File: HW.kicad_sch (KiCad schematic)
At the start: 0 parts

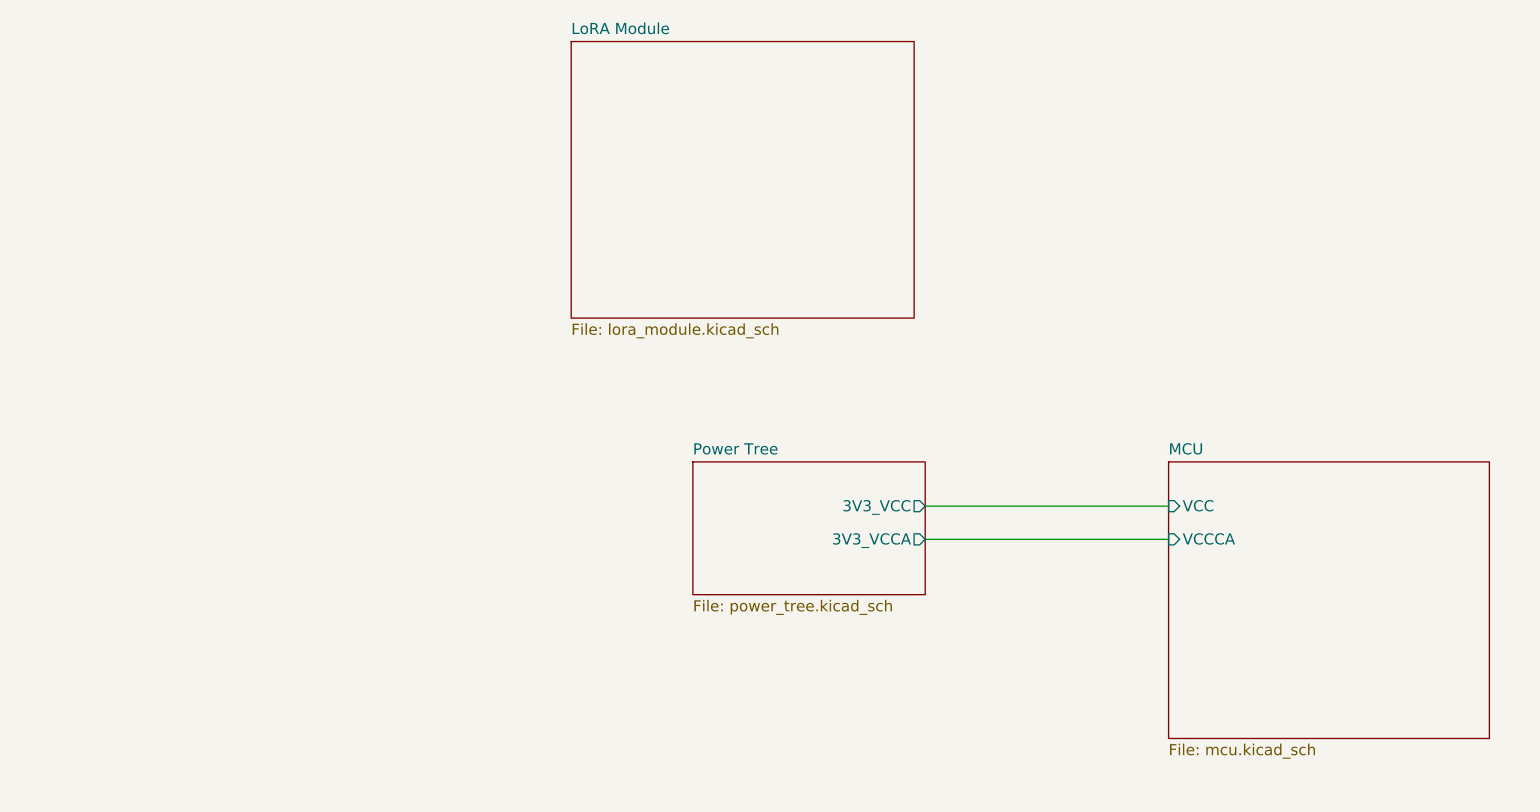
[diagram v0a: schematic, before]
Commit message: feat(usb-uart): add FT232RL USB‑UART bridge and wire RX/TX to MCU
Added the FT232RL USB‑to‑UART interface IC (FT232RL) into the schematic and powered it from the 3.3 V and 5 V rails. Exposed its TTL-level RXD and TXD pins through the hierarchical sheet and connected it to the MCU

- Placed FT232RL SSOP‑28 symbol and footprint, tied VCCIO to 3.3 V, VCC to USB_VCC, and GND to ground.
- Left legacy RS‑232 control lines (DSR#, DCD#, RI#) and CBUS pins unconnected.
- Updated hierarchy:added sheet pins on USB_UART page.

This enables USB‑serial communication between host PC and STM32F030F4Px
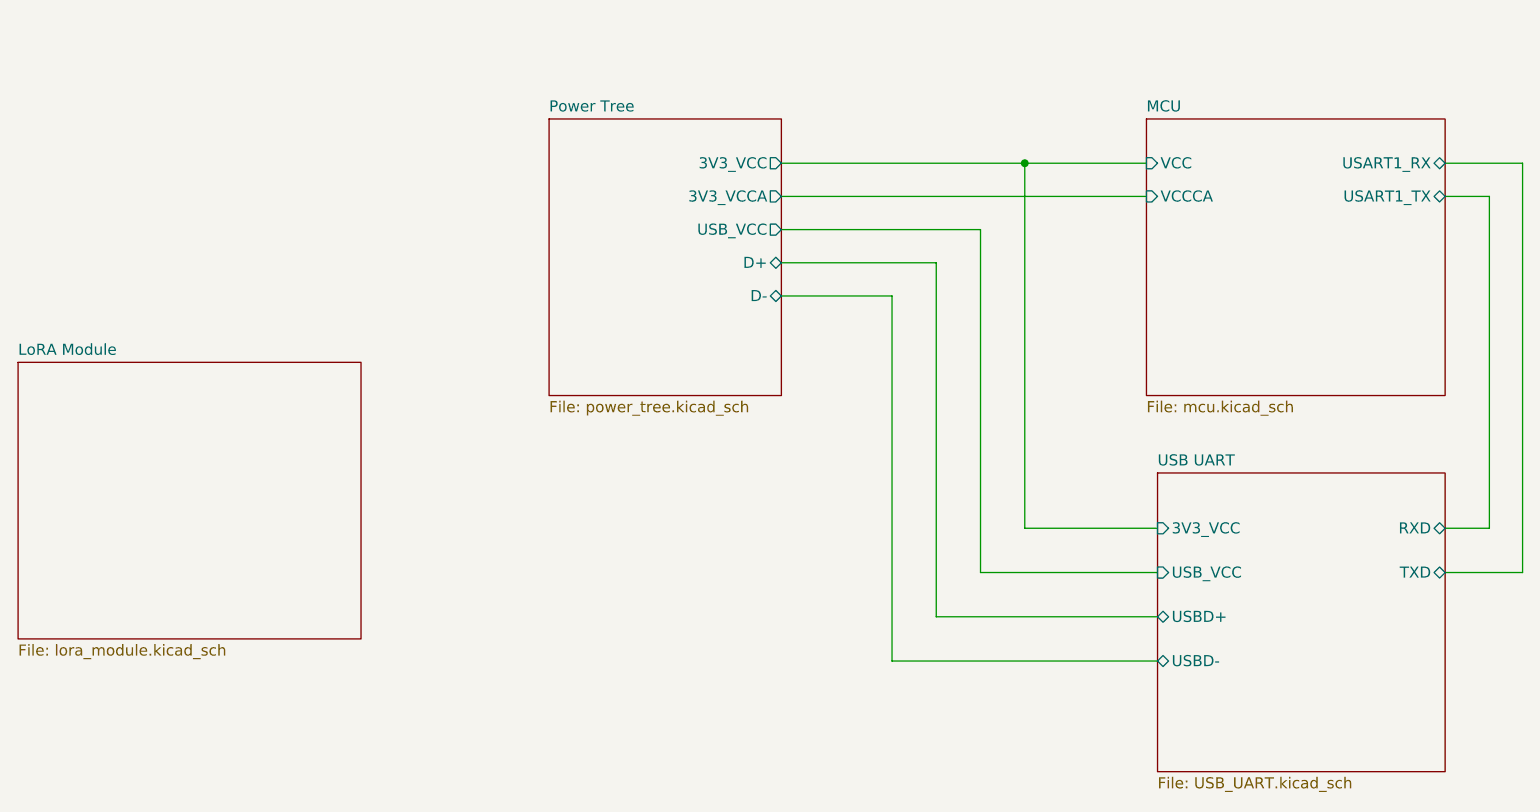
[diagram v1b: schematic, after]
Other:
- added sheet USB UART (USB_UART.kicad_sch)
- sheet MCU ports: added USART1_RX, USART1_TX; removed none
- sheet Power Tree ports: added D+, D-, USB_VCC; removed none

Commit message: feat(usb-uart): add FT232RL for USB-serial, update schematic and layout
Added FT232RL USB‑to‑UART interface IC, powered from 3.3 V and 5 V rails. Connected RXD and TXD to MCU via hierarchical sheet. Left RS‑232 control lines and CBUS pins unconnected. Updated hierarchy with USB_UART sheet pins.

BREAKING CHANGE: USB connector moved to USB_UART sheet; schematic wiring changed to bus-based layout. AGND now kept in separate plane using GNDA power symbol in KiCad.
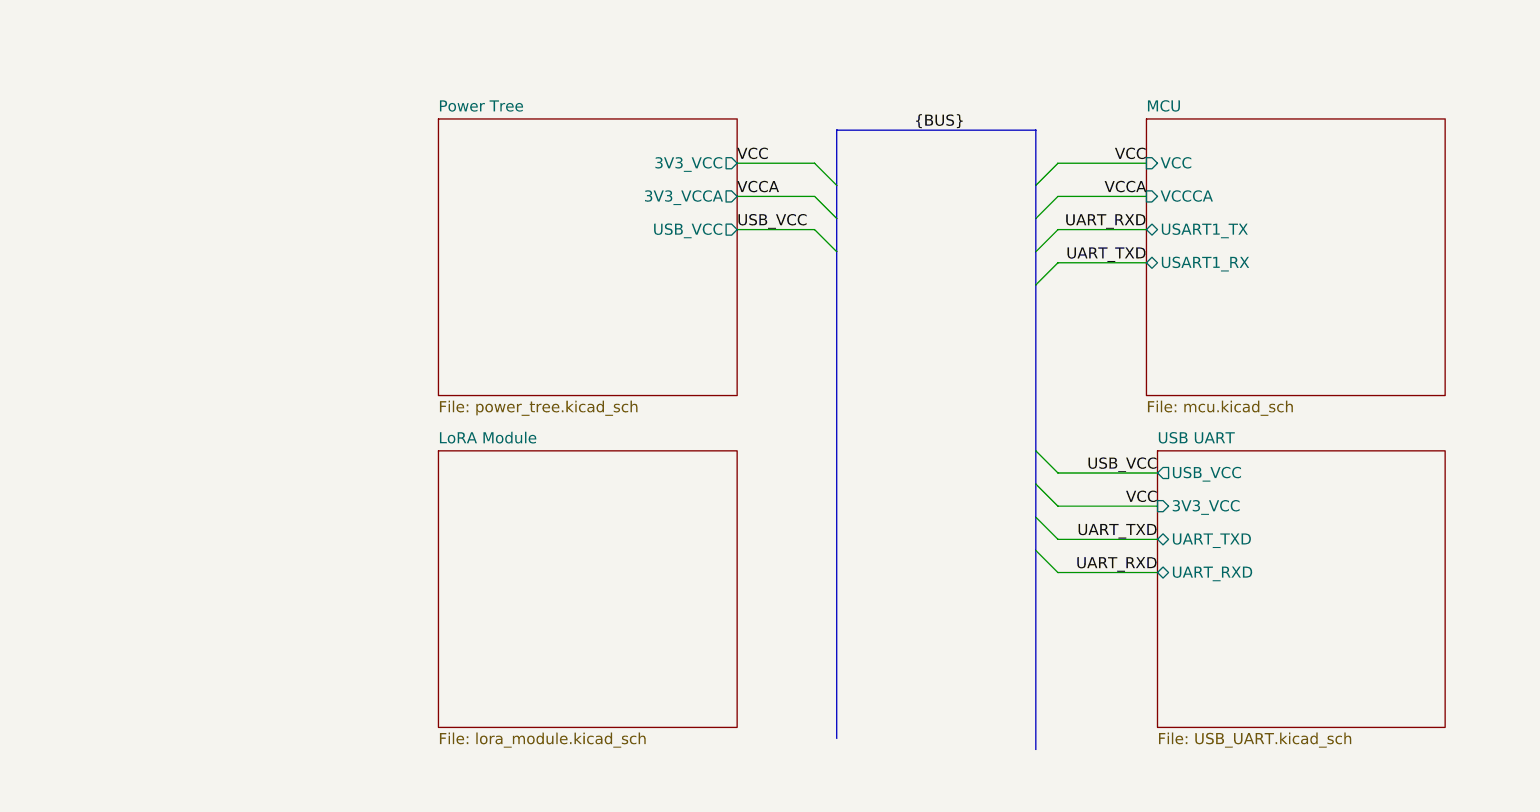
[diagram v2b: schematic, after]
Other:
- sheet Power Tree ports: added none; removed D+, D-
- sheet USB UART ports: added UART_RXD, UART_TXD; removed RXD, TXD, USBD+, USBD-

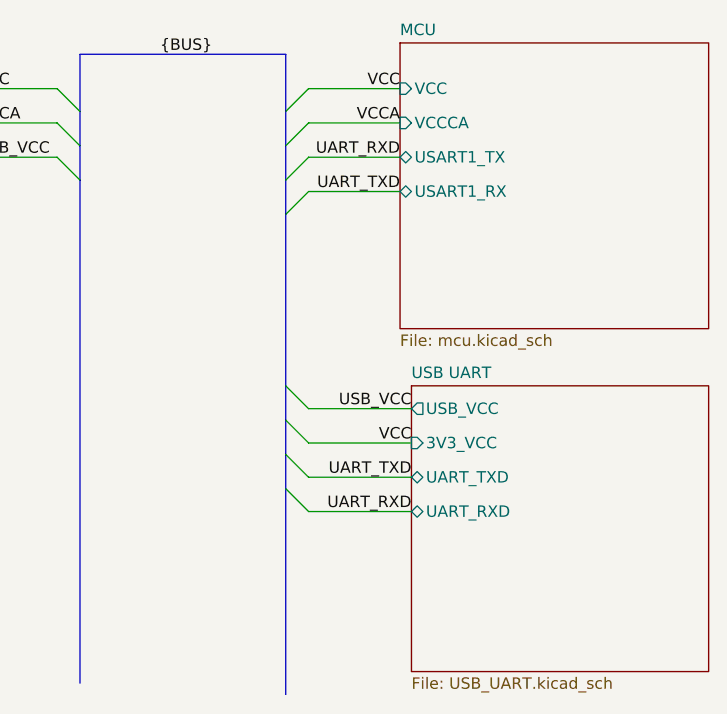
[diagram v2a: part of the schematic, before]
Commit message: fix: Separted CC1 and CC2 resistors and fixed the UART label directions
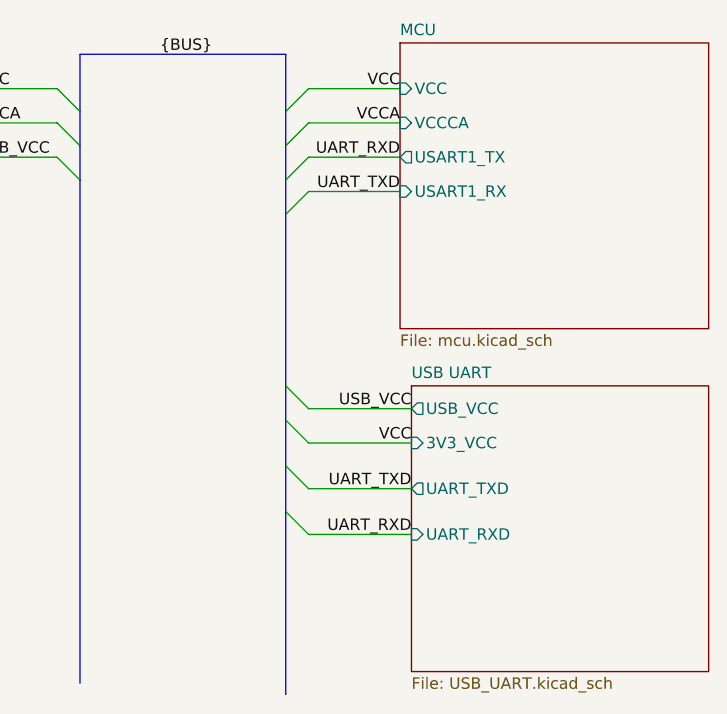
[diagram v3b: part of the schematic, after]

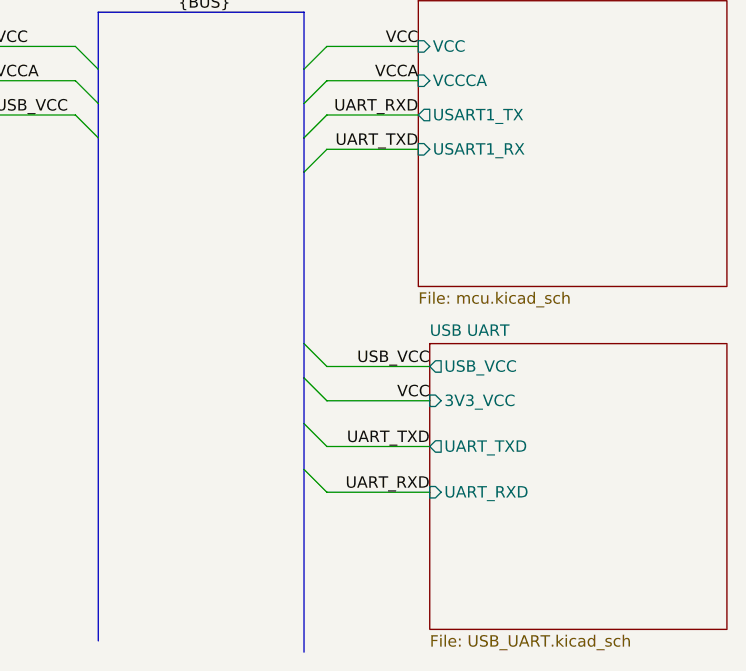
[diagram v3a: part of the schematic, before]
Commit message: feat(FT232RL_Reset): Added FT232RL Reset functionality using the Reset switch
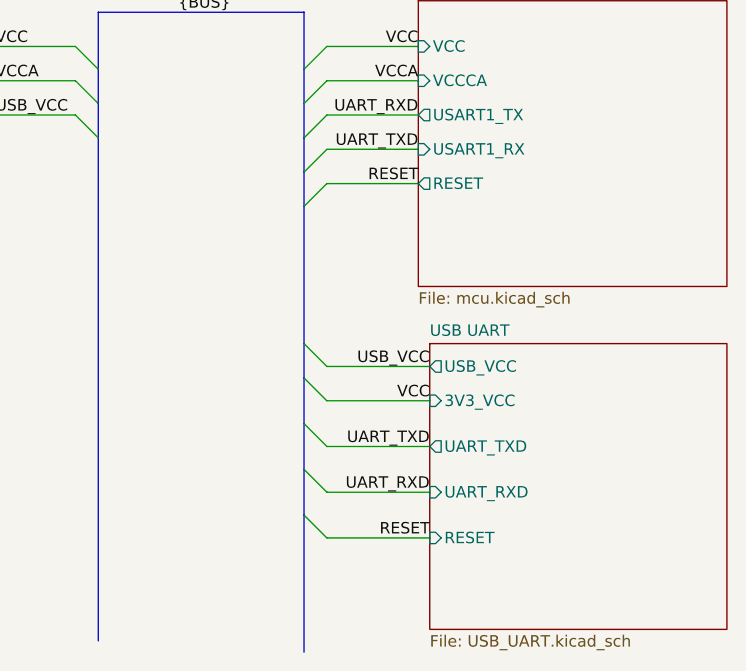
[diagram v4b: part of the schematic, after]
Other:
- sheet MCU ports: added RESET; removed none
- sheet USB UART ports: added RESET; removed none
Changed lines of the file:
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@@
 	(paper "A4")
 	(bus_alias "BUS"
-		(members "VCC " "VCCA" "UART_TXD" "UART_RXD" "USB_VCC")
+		(members "VCC " "VCCA" "UART_TXD" "UART_RXD" "USB_VCC" "RESET")
 	)
 	(bus_entry
@@
 	)
 	(bus_entry
+		(at 147.32 113.03)
+		(size 2.54 2.54)
+		(stroke
+			(width 0)
+			(type default)
+		)
+	)
+	(bus_entry
 		(at 147.32 67.31)
 		(size 2.54 -2.54)
@@
 	)
 	(bus_entry
+		(at 147.32 78.74)
+		(size 2.54 -2.54)
+		(stroke
+			(width 0)
+			(type default)
+		)
+	)
+	(bus_entry
 		(at 124.46 71.12)
 		(size -2.54 -2.54)
@@
 		)
 	)
+	(bus
+		(pts
+			(xy 147.32 78.74) (xy 147.32 93.98)
+		)
+		(stroke
+			(width 0)
+			(type default)
+		)
+	)
 	(wire
 		(pts
@@
 	(bus
 		(pts
+			(xy 147.32 113.03) (xy 147.32 128.27)
+		)
+		(stroke
+			(width 0)
+			(type default)
+		)
+	)
+	(wire
+		(pts
+			(xy 149.86 76.2) (xy 160.02 76.2)
+		)
+		(stroke
+			(width 0)
+			(type default)
+		)
+	)
+	(bus
+		(pts
 			(xy 124.46 67.31) (xy 124.46 63.5)
 		)
@@
 	(wire
 		(pts
+			(xy 149.86 115.57) (xy 161.29 115.57)
+		)
+		(stroke
+			(width 0)
+			(type default)
+		)
+	)
+	(wire
+		(pts
 			(xy 149.86 68.58) (xy 160.02 68.58)
 		)
@@
 	(bus
 		(pts
-			(xy 147.32 74.93) (xy 147.32 93.98)
+			(xy 147.32 74.93) (xy 147.32 78.74)
 		)
 		(stroke
@@
 	(bus
 		(pts
-			(xy 147.32 107.95) (xy 147.32 128.27)
+			(xy 147.32 107.95) (xy 147.32 113.03)
 		)
 		(stroke
@@
 		)
 	)
+	(label "RESET"
+		(at 160.02 76.2 180)
+		(effects
+			(font
+				(size 1.27 1.27)
+			)
+			(justify right bottom)
+		)
+	)
 	(label "VCC "
 		(at 113.03 60.96 0)
@@
 			)
 			(justify left bottom)
+		)
+	)
+	(label "RESET"
+		(at 161.29 115.57 180)
+		(effects
+			(font
+				(size 1.27 1.27)
+			)
+			(justify right bottom)
 		)
 	)
@@
 			)
 		)
+		(pin "RESET" input
+			(at 161.29 115.57 180)
+			(effects
+				(font
+					(size 1.27 1.27)
+				)
+				(justify left)
+			)
+		)
 		(instances
 			(project "HW"
@@
 			(effects
 				(font
+					(size 1.27 1.27)
+				)
+				(justify left)
+			)
+		)
+		(pin "RESET" output
+			(at 160.02 76.2 180)
+			(effects
+				(font
